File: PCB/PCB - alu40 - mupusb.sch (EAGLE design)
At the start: 160 parts, among them IC1 XB3303ASOT23, IC2 TP4054-42-SOT25-R, J1 SK-3296S-01-L1, Q2 PMOSFET, Q3 PMOSFET, Q5 PMOSFET, Q6 NMOSFET, U1 ISP1807-LRISP1807-LR_ISP1807-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, X1 BM02B-SRSS-TB

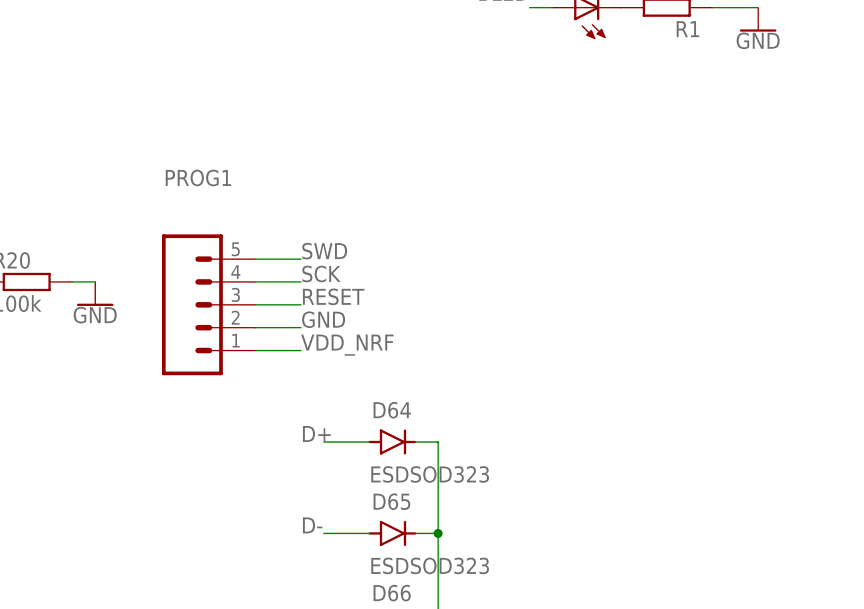
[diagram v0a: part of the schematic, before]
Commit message: Add Tagconnect and thermal relif for tp4054
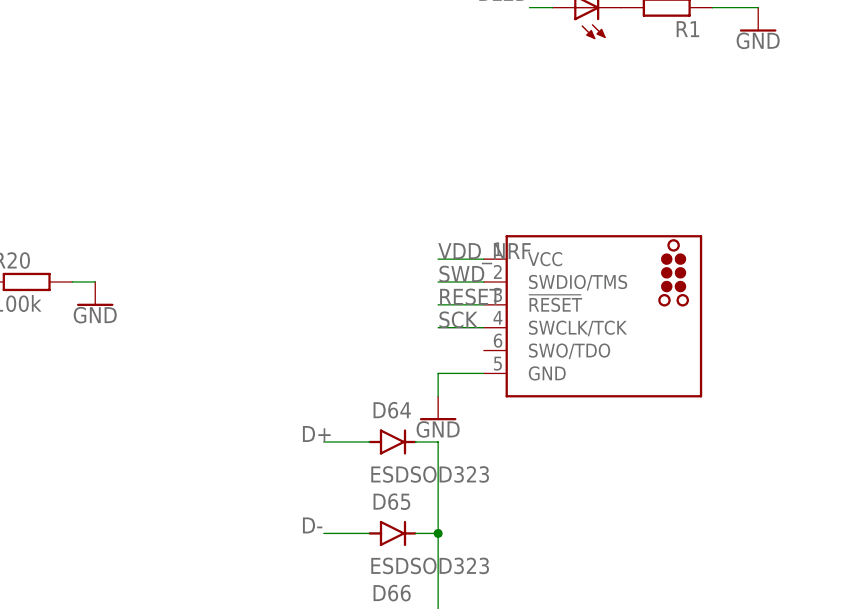
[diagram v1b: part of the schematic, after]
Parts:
- removed PROG1: (no value), SparkFun-Connectors:CONN_051.27MM
- added J2: (no value), tag-connect:TC2030_SWD-MCP-NL
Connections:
- net GND: now also J2.GND; no longer PROG1.2
- net RESET: now also J2.!RESET; no longer PROG1.3
- net SCK: now also J2.SWCLK/TCK; no longer PROG1.4
- net SWD: now also J2.SWDIO/TMS; no longer PROG1.5
- net VDD_NRF: now also J2.VCC; no longer PROG1.1
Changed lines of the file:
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@@
 <part name="GND31" library="SparkFun-PowerSymbols" library_urn="urn:adsk.eagle:library:530" deviceset="GND" device=""/>
 <part name="SUPPLY17" library="SparkFun-PowerSymbols" library_urn="urn:adsk.eagle:library:530" deviceset="V_BATT" device=""/>
-<part name="PROG1" library="SparkFun-Connectors" library_urn="urn:adsk.eagle:library:513" deviceset="CONN_05" device="1.27MM" package3d_urn="urn:adsk.eagle:package:38110/1"/>
 <part name="LED1" library="adafruit" library_urn="urn:adsk.eagle:library:420" deviceset="LED" device="CHIPLED_0805" package3d_urn="urn:adsk.eagle:package:6240559/1" value="RED"/>
 <part name="R1" library="rcl" library_urn="urn:adsk.eagle:library:334" deviceset="R-EU_" device="R0603" package3d_urn="urn:adsk.eagle:package:23555/3" value="200"/>
@@
 <part name="GND26" library="SparkFun-PowerSymbols" library_urn="urn:adsk.eagle:library:530" deviceset="GND" device=""/>
 <part name="SUPPLY1" library="SparkFun-PowerSymbols" library_urn="urn:adsk.eagle:library:530" deviceset="V_USB" device=""/>
+<part name="J2" library="tag-connect" deviceset="TC2030_SWD" device="-MCP-NL"/>
+<part name="GND3" library="SparkFun-PowerSymbols" library_urn="urn:adsk.eagle:library:530" deviceset="GND" device=""/>
 </parts>
 <sheets>
@@
 <attribute name="VALUE" x="-381" y="-40.386" size="1.778" layer="96" align="bottom-center"/>
 </instance>
-<instance part="PROG1" gate="G$1" x="-340.36" y="-45.72" smashed="yes">
-<attribute name="VALUE" x="-342.9" y="-55.626" size="1.778" layer="96" font="vector"/>
-<attribute name="NAME" x="-342.9" y="-32.512" size="1.778" layer="95" font="vector"/>
-</instance>
 <instance part="LED1" gate="G$1" x="-297.18" y="-12.7" smashed="yes" rot="R90">
 <attribute name="NAME" x="-292.608" y="-9.144" size="1.778" layer="95" rot="R180"/>
@@
 <attribute name="VALUE" x="-571.5" y="-2.286" size="1.778" layer="96" align="bottom-center"/>
 </instance>
+<instance part="J2" gate="G$1" x="-294.64" y="-48.26" smashed="yes"/>
+<instance part="GND3" gate="1" x="-312.42" y="-58.42" smashed="yes">
+<attribute name="VALUE" x="-312.42" y="-58.674" size="1.778" layer="96" align="top-center"/>
+</instance>
 </instances>
 <busses>
@@
 </segment>
 <segment>
-<pinref part="PROG1" gate="G$1" pin="5"/>
-<wire x1="-332.74" y1="-40.64" x2="-327.66" y2="-40.64" width="0.1524" layer="91"/>
-<label x="-327.66" y="-40.64" size="1.778" layer="95"/>
+<label x="-312.42" y="-43.18" size="1.778" layer="95"/>
+<pinref part="J2" gate="G$1" pin="SWDIO/TMS"/>
+<wire x1="-307.34" y1="-43.18" x2="-312.42" y2="-43.18" width="0.1524" layer="91"/>
 </segment>
 </net>
@@
 </segment>
 <segment>
-<pinref part="PROG1" gate="G$1" pin="4"/>
-<wire x1="-332.74" y1="-43.18" x2="-327.66" y2="-43.18" width="0.1524" layer="91"/>
-<label x="-327.66" y="-43.18" size="1.778" layer="95"/>
+<pinref part="J2" gate="G$1" pin="SWCLK/TCK"/>
+<wire x1="-307.34" y1="-48.26" x2="-312.42" y2="-48.26" width="0.1524" layer="91"/>
+<label x="-312.42" y="-48.26" size="1.778" layer="95"/>
 </segment>
 </net>
@@
 </segment>
 <segment>
-<pinref part="PROG1" gate="G$1" pin="3"/>
-<wire x1="-332.74" y1="-45.72" x2="-327.66" y2="-45.72" width="0.1524" layer="91"/>
-<label x="-327.66" y="-45.72" size="1.778" layer="95"/>
-</segment>
-<segment>
 <pinref part="R2" gate="G$1" pin="2"/>
 <wire x1="-454.66" y1="20.32" x2="-457.2" y2="20.32" width="0.1524" layer="91"/>
@@
 <label x="-160.02" y="-78.74" size="1.778" layer="95" rot="R270"/>
 </segment>
+<segment>
+<pinref part="J2" gate="G$1" pin="!RESET"/>
+<wire x1="-307.34" y1="-45.72" x2="-312.42" y2="-45.72" width="0.1524" layer="91"/>
+<label x="-312.42" y="-45.72" size="1.778" layer="95"/>
+</segment>
 </net>
 <net name="POWER_PIN" class="0">
@@
 </segment>
 <segment>
-<pinref part="PROG1" gate="G$1" pin="1"/>
-<wire x1="-332.74" y1="-50.8" x2="-327.66" y2="-50.8" width="0.1524" layer="91"/>
-<label x="-327.66" y="-50.8" size="1.778" layer="95"/>
-</segment>
-<segment>
 <wire x1="-439.42" y1="22.86" x2="-439.42" y2="20.32" width="0.1524" layer="91"/>
 <pinref part="R2" gate="G$1" pin="1"/>
@@
 <label x="-388.62" y="-88.9" size="1.778" layer="95"/>
 </segment>
+<segment>
+<pinref part="J2" gate="G$1" pin="VCC"/>
+<wire x1="-307.34" y1="-40.64" x2="-312.42" y2="-40.64" width="0.1524" layer="91"/>
+<label x="-312.42" y="-40.64" size="1.778" layer="95"/>
+</segment>
 </net>
 <net name="D-" class="0">
@@
 <pinref part="GND31" gate="1" pin="GND"/>
 <wire x1="-353.06" y1="-43.18" x2="-350.52" y2="-43.18" width="0.1524" layer="91"/>
-</segment>
-<segment>
-<pinref part="PROG1" gate="G$1" pin="2"/>
-<wire x1="-332.74" y1="-48.26" x2="-327.66" y2="-48.26" width="0.1524" layer="91"/>
-<label x="-327.66" y="-48.26" size="1.778" layer="95"/>
 </segment>
 <segment>
@@
 <pinref part="R12" gate="G$1" pin="1"/>
 </segment>
-</net>
+<segment>
+<pinref part="J2" gate="G$1" pin="GND"/>
+<wire x1="-307.34" y1="-53.34" x2="-312.42" y2="-53.34" width="0.1524" layer="91"/>
+<wire x1="-312.42" y1="-53.34" x2="-312.42" y2="-55.88" width="0.1524" layer="91"/>
+<pinref part="GND3" gate="1" pin="GND"/>
+</segment>
+</net>

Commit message: most of new updates
Needs new reset and power switch, new USB port
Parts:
- removed 112ENC: ENCODERHOLE, Volume_V1:ENCODERHOLE
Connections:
- net A: no longer 112ENC.A
- net B: no longer 112ENC.B
- net COL11: no longer 112ENC.S2
- net GND: no longer 112ENC.GND
- net N$12: no longer 112ENC.S1
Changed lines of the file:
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@@
 <part name="U$10" library="Volume_V1" library_urn="urn:adsk.eagle:library:32198814" deviceset="STAB-2U" device="" package3d_urn="urn:adsk.eagle:package:32198944/1"/>
 <part name="11ENC" library="Volume_V1" library_urn="urn:adsk.eagle:library:32198814" deviceset="ENCODER" device="HOLE" package3d_urn="urn:adsk.eagle:package:32198968/1"/>
-<part name="112ENC" library="Volume_V1" library_urn="urn:adsk.eagle:library:32198814" deviceset="ENCODER" device="HOLE" package3d_urn="urn:adsk.eagle:package:32198968/1"/>
 <part name="41ENC\" library="Volume_V1" library_urn="urn:adsk.eagle:library:32198814" deviceset="ENCODER" device="HOLE" package3d_urn="urn:adsk.eagle:package:32198968/1"/>
 <part name="412ENC" library="Volume_V1" library_urn="urn:adsk.eagle:library:32198814" deviceset="ENCODER" device="HOLE" package3d_urn="urn:adsk.eagle:package:32198968/1"/>
 <part name="GND5" library="SparkFun-PowerSymbols" library_urn="urn:adsk.eagle:library:530" deviceset="GND" device=""/>
 <part name="GND7" library="SparkFun-PowerSymbols" library_urn="urn:adsk.eagle:library:530" deviceset="GND" device=""/>
-<part name="GND14" library="SparkFun-PowerSymbols" library_urn="urn:adsk.eagle:library:530" deviceset="GND" device=""/>
 <part name="GND15" library="SparkFun-PowerSymbols" library_urn="urn:adsk.eagle:library:530" deviceset="GND" device=""/>
 <part name="45-2" library="Volume_V1" library_urn="urn:adsk.eagle:library:32198814" deviceset="CHERRY" device="" package3d_urn="urn:adsk.eagle:package:32198958/1"/>
@@
 <instance part="U$10" gate="G$1" x="-259.08" y="-81.28" smashed="yes"/>
 <instance part="11ENC" gate="G$1" x="0" y="12.7" smashed="yes"/>
-<instance part="112ENC" gate="G$1" x="279.4" y="12.7" smashed="yes"/>
 <instance part="41ENC\" gate="G$1" x="0" y="-139.7" smashed="yes"/>
 <instance part="412ENC" gate="G$1" x="279.4" y="-139.7" smashed="yes"/>
@@
 <instance part="GND7" gate="1" x="0" y="30.48" smashed="yes" rot="R180">
 <attribute name="VALUE" x="0" y="30.734" size="1.778" layer="96" rot="R180" align="top-center"/>
-</instance>
-<instance part="GND14" gate="1" x="279.4" y="30.48" smashed="yes" rot="R180">
-<attribute name="VALUE" x="279.4" y="30.734" size="1.778" layer="96" rot="R180" align="top-center"/>
 </instance>
 <instance part="GND15" gate="1" x="279.4" y="-121.92" smashed="yes" rot="R180">
@@
 <wire x1="269.24" y1="0" x2="269.24" y2="-2.54" width="0.1524" layer="91"/>
 <pinref part="112" gate="SW" pin="1"/>
-<pinref part="112ENC" gate="G$1" pin="S1"/>
 <wire x1="266.7" y1="10.16" x2="266.7" y2="0" width="0.1524" layer="91"/>
 <wire x1="266.7" y1="0" x2="269.24" y2="0" width="0.1524" layer="91"/>
@@
 <pinref part="11ENC" gate="G$1" pin="GND"/>
 <pinref part="GND7" gate="1" pin="GND"/>
-</segment>
-<segment>
-<pinref part="112ENC" gate="G$1" pin="GND"/>
-<pinref part="GND14" gate="1" pin="GND"/>
 </segment>
 <segment>
@@
 <wire x1="292.1" y1="-137.16" x2="289.56" y2="-137.16" width="0.1524" layer="91"/>
 <junction x="289.56" y="-137.16"/>
-<pinref part="112ENC" gate="G$1" pin="S2"/>
 <wire x1="292.1" y1="10.16" x2="292.1" y2="0" width="0.1524" layer="91"/>
 <wire x1="292.1" y1="0" x2="289.56" y2="0" width="0.1524" layer="91"/>
@@
 </segment>
 <segment>
-<pinref part="112ENC" gate="G$1" pin="A"/>
-<wire x1="274.32" y1="27.94" x2="274.32" y2="33.02" width="0.1524" layer="91"/>
-<wire x1="274.32" y1="35.56" x2="274.32" y2="33.02" width="0.1524" layer="91"/>
-<label x="274.32" y="35.56" size="1.778" layer="95"/>
-</segment>
-<segment>
 <pinref part="11ENC" gate="G$1" pin="A"/>
 <wire x1="-5.08" y1="27.94" x2="-5.08" y2="33.02" width="0.1524" layer="91"/>
@@
 </segment>
 <segment>
-<pinref part="112ENC" gate="G$1" pin="B"/>
-<wire x1="284.48" y1="27.94" x2="284.48" y2="35.56" width="0.1524" layer="91"/>
-<label x="284.48" y="35.56" size="1.778" layer="95"/>
-</segment>
-<segment>

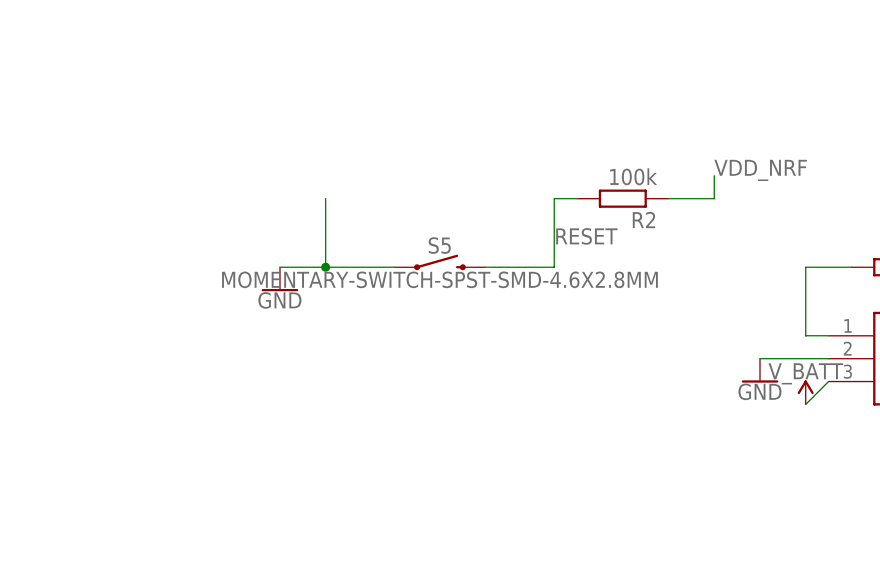
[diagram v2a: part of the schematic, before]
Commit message: Route new switch footprints
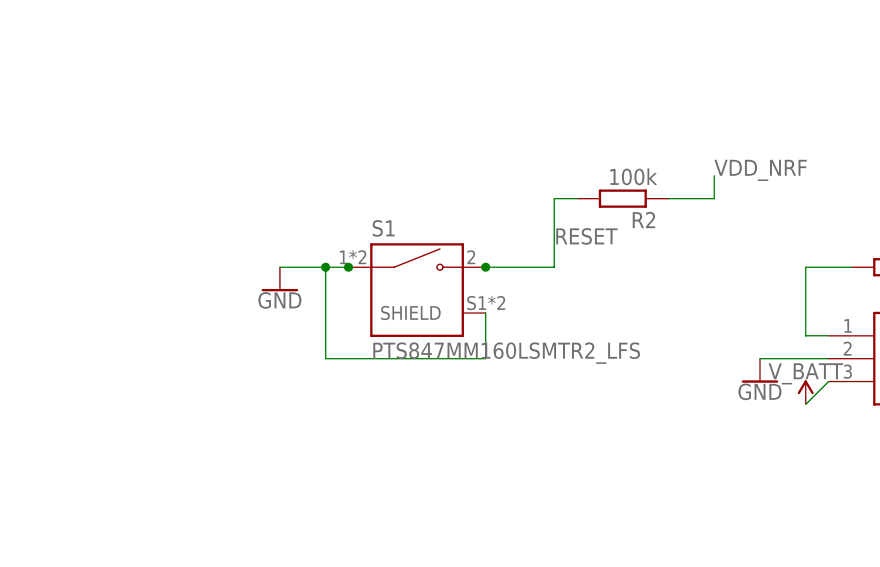
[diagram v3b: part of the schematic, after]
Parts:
- removed S5: MOMENTARY-SWITCH-SPST-SMD-4.6X2.8MM, Volume_V1:MOMENTARY-SWITCH-SPST-SMD-4.6X2.8MM
- added S1: PTS847MM160LSMTR2_LFS, PTS847MM160LSMTR2_LFS:PTS847MM160LSMTR2_LFS
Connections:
- net GND: now also S1.COM, S1.SHIELD; no longer S5.1
- net RESET: now also S1.NO; no longer S5.2
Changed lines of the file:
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@@
 <part name="GND13" library="SparkFun-PowerSymbols" library_urn="urn:adsk.eagle:library:530" deviceset="GND" device=""/>
 <part name="IC2" library="TP4054-42-SOT25-R" deviceset="TP4054-42-SOT25-R" device=""/>
-<part name="S5" library="Volume_V1" library_urn="urn:adsk.eagle:library:32198814" deviceset="MOMENTARY-SWITCH-SPST" device="-SMD-4.6X2.8MM" package3d_urn="urn:adsk.eagle:package:32213842/2"/>
 <part name="Q5" library="Transistor" library_urn="urn:adsk.eagle:library:16378713" deviceset="PMOSFET" device="SOT23" package3d_urn="urn:adsk.eagle:package:28738/2" technology="_" value="PMOSFET">
 <attribute name="MPN" value="SL2301S"/>
@@
 <part name="D51" library="Volume_V1" library_urn="urn:adsk.eagle:library:32198814" deviceset="1N4148WS" device="" package3d_urn="urn:adsk.eagle:package:32198954/3"/>
 <part name="D52" library="Volume_V1" library_urn="urn:adsk.eagle:library:32198814" deviceset="1N4148WS" device="" package3d_urn="urn:adsk.eagle:package:32198954/3"/>
-<part name="J3" library="Volume_V1" library_urn="urn:adsk.eagle:library:32198814" deviceset="SPARKFUN-CONNECTORS_USB_C" device=""/>
+<part name="J3" library="Volume_V1" library_urn="urn:adsk.eagle:library:32198814" deviceset="SPARKFUN-CONNECTORS_USB_C" device="" package3d_urn="urn:adsk.eagle:package:40549079/1"/>
 <part name="GND21" library="SparkFun-PowerSymbols" library_urn="urn:adsk.eagle:library:530" deviceset="GND" device=""/>
 <part name="GND25" library="SparkFun-PowerSymbols" library_urn="urn:adsk.eagle:library:530" deviceset="GND" device=""/>
@@
 <part name="J2" library="tag-connect" deviceset="TC2030_SWD" device="-MCP-NL"/>
 <part name="GND3" library="SparkFun-PowerSymbols" library_urn="urn:adsk.eagle:library:530" deviceset="GND" device=""/>
+<part name="S1" library="PTS847MM160LSMTR2_LFS" deviceset="PTS847MM160LSMTR2_LFS" device=""/>
 </parts>
 <sheets>
@@
 <attribute name="VALUE" x="-400.05" y="10.16" size="1.778" layer="96" align="center-left"/>
 </instance>
-<instance part="S5" gate="G$1" x="-469.9" y="12.7" smashed="yes">
-<attribute name="NAME" x="-469.9" y="14.224" size="1.778" layer="95" font="vector" align="bottom-center"/>
-<attribute name="VALUE" x="-469.9" y="12.192" size="1.778" layer="96" font="vector" align="top-center"/>
-</instance>
 <instance part="Q5" gate="G$1" x="-421.64" y="-83.82" smashed="yes" rot="MR180">
 <attribute name="NAME" x="-415.29" y="-85.09" size="1.778" layer="95" rot="MR180"/>
@@
 <instance part="GND3" gate="1" x="-312.42" y="-58.42" smashed="yes">
 <attribute name="VALUE" x="-312.42" y="-58.674" size="1.778" layer="96" align="top-center"/>
+</instance>
+<instance part="S1" gate="G$1" x="-472.44" y="10.16" smashed="yes">
+<attribute name="NAME" x="-477.52" y="16.129" size="1.778" layer="95"/>
+<attribute name="VALUE" x="-477.52" y="2.54" size="1.778" layer="96"/>
 </instance>
 </instances>
@@
 <label x="-457.2" y="15.24" size="1.778" layer="95"/>
 <wire x1="-457.2" y1="20.32" x2="-457.2" y2="12.7" width="0.1524" layer="91"/>
-<pinref part="S5" gate="G$1" pin="2"/>
+<pinref part="S1" gate="G$1" pin="NO"/>
 <wire x1="-464.82" y1="12.7" x2="-457.2" y2="12.7" width="0.1524" layer="91"/>
+<junction x="-464.82" y="12.7"/>
 </segment>
 <segment>
@@
 <segment>
 <pinref part="GND2" gate="1" pin="GND"/>
+<pinref part="S1" gate="G$1" pin="COM"/>
+<wire x1="-480.06" y1="12.7" x2="-482.6" y2="12.7" width="0.1524" layer="91"/>
+<junction x="-480.06" y="12.7"/>
+<pinref part="S1" gate="G$1" pin="SHIELD"/>
 <wire x1="-482.6" y1="12.7" x2="-487.68" y2="12.7" width="0.1524" layer="91"/>
-<wire x1="-482.6" y1="20.32" x2="-482.6" y2="12.7" width="0.1524" layer="91"/>
-<pinref part="S5" gate="G$1" pin="1"/>
-<wire x1="-474.98" y1="12.7" x2="-482.6" y2="12.7" width="0.1524" layer="91"/>
+<wire x1="-464.82" y1="7.62" x2="-464.82" y2="2.54" width="0.1524" layer="91"/>
+<wire x1="-464.82" y1="2.54" x2="-482.6" y2="2.54" width="0.1524" layer="91"/>
+<wire x1="-482.6" y1="2.54" x2="-482.6" y2="12.7" width="0.1524" layer="91"/>
 <junction x="-482.6" y="12.7"/>
 </segment>
